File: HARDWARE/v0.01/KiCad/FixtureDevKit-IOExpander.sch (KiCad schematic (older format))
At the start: 58 parts, among them J57 IOExp_0, J58 IOExp_0, J59 Conn_01x24, J60 IOExp_1, J61 IOExp_1, J62 Conn_01x24, U5 TCA6426A, U6 TCA6426A

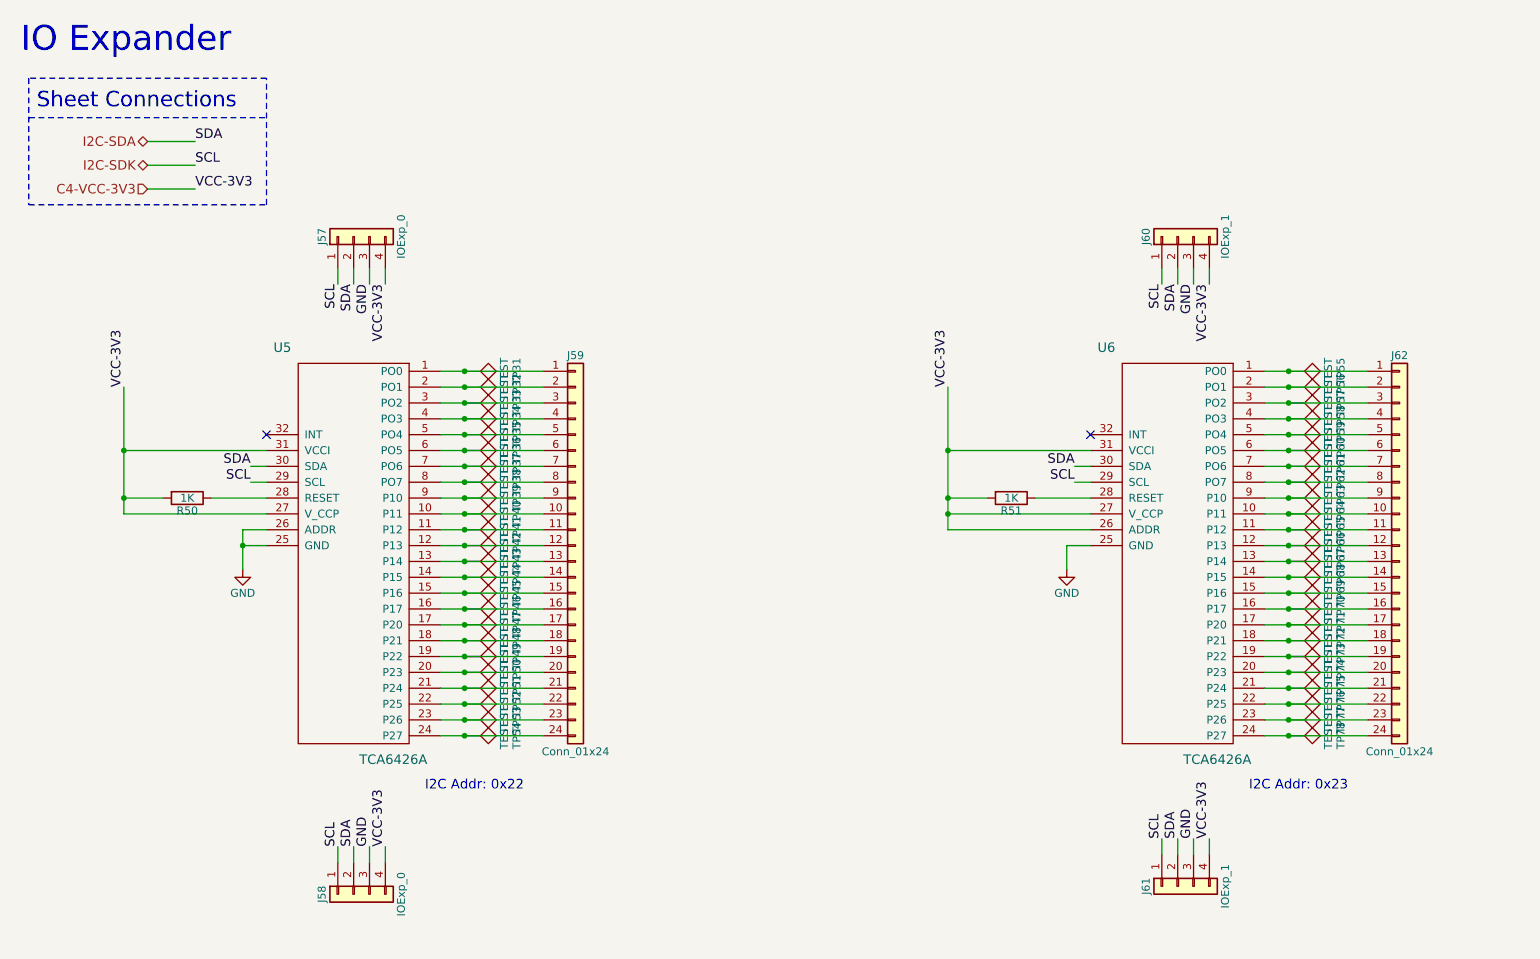
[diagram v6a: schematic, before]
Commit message: adding footprints, starting layout
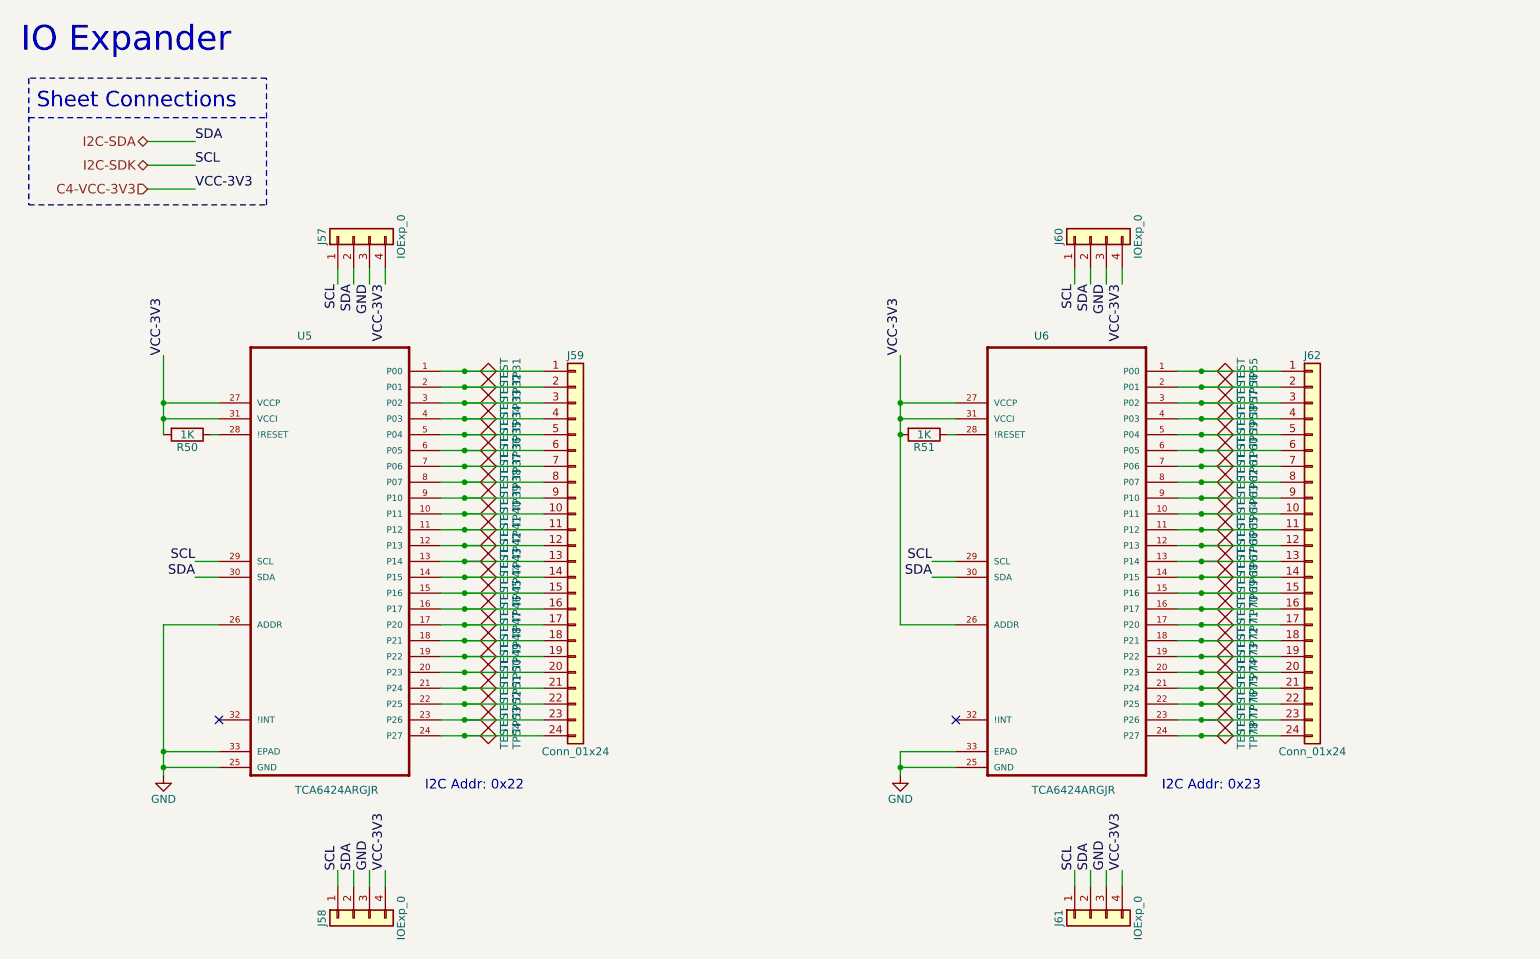
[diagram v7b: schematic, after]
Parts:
- removed U5, U6: TCA6426A, symbol TCA6426A
- added U5, U6: TCA6424ARGJR, TCA6424ARGJR:QFN50P500X500X60-33N, symbol TCA6424ARGJR
- J60, J61: value IOExp_1 -> IOExp_0
- TP31, TP32, TP33, TP34, TP35, TP36, TP37, TP38, TP39, TP40, TP41, TP42, TP43, TP44, TP45, TP46, TP47, TP48, TP49, TP50, TP51, TP52, TP53, TP54, TP55, TP56, TP57, TP58, TP59, TP60, TP61, TP62, TP63, TP64, TP65, TP66, TP67, TP68, TP69, TP70, TP71, TP72, TP73, TP74, TP75, TP76, TP77, TP78: footprint (none) -> TestPoint:TestPoint
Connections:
- net C4-VCC-3V3: now also U5.27 (VCCP), U5.31 (VCCI), U6.26 (ADDR), U6.27 (VCCP), U6.31 (VCCI)
- net GND: now also U5.25 (GND), U5.26 (ADDR), U5.33 (EPAD), U6.25 (GND), U6.33 (EPAD)
- net I2C-SDA: now also U5.30 (SDA), U6.30 (SDA)
- net I2C-SDK: now also U5.29 (SCL), U6.29 (SCL)
- net at J59.1 (Pin_1), TP31.1: now also U5.1 (P00)
- net at J59.10 (Pin_10), TP40.1: now also U5.10 (P11)
- net at J59.11 (Pin_11), TP41.1: now also U5.11 (P12)
- net at J59.12 (Pin_12), TP42.1: now also U5.12 (P13)
- net at J59.13 (Pin_13), TP43.1: now also U5.13 (P14)
- net at J59.14 (Pin_14), TP44.1: now also U5.14 (P15)
- net at J59.15 (Pin_15), TP45.1: now also U5.15 (P16)
- net at J59.16 (Pin_16), TP46.1: now also U5.16 (P17)
- net at J59.17 (Pin_17), TP47.1: now also U5.17 (P20)
- net at J59.18 (Pin_18), TP48.1: now also U5.18 (P21)
- net at J59.19 (Pin_19), TP49.1: now also U5.19 (P22)
- net at J59.2 (Pin_2), TP32.1: now also U5.2 (P01)
- net at J59.20 (Pin_20), TP50.1: now also U5.20 (P23)
- net at J59.21 (Pin_21), TP51.1: now also U5.21 (P24)
- net at J59.22 (Pin_22), TP52.1: now also U5.22 (P25)
- net at J59.23 (Pin_23), TP53.1: now also U5.23 (P26)
- net at J59.24 (Pin_24), TP54.1: now also U5.24 (P27)
- net at R50.1: now also U5.28 (!RESET)
- net at J59.3 (Pin_3), TP33.1: now also U5.3 (P02)
- net at J59.4 (Pin_4), TP34.1: now also U5.4 (P03)
- net at J59.5 (Pin_5), TP35.1: now also U5.5 (P04)
- net at J59.6 (Pin_6), TP36.1: now also U5.6 (P05)
- net at J59.7 (Pin_7), TP37.1: now also U5.7 (P06)
- net at J59.8 (Pin_8), TP38.1: now also U5.8 (P07)
- net at J59.9 (Pin_9), TP39.1: now also U5.9 (P10)
- net at J62.1 (Pin_1), TP55.1: now also U6.1 (P00)
- net at J62.10 (Pin_10), TP64.1: now also U6.10 (P11)
- net at J62.11 (Pin_11), TP65.1: now also U6.11 (P12)
- net at J62.12 (Pin_12), TP66.1: now also U6.12 (P13)
- net at J62.13 (Pin_13), TP67.1: now also U6.13 (P14)
- net at J62.14 (Pin_14), TP68.1: now also U6.14 (P15)
- net at J62.15 (Pin_15), TP69.1: now also U6.15 (P16)
- net at J62.16 (Pin_16), TP70.1: now also U6.16 (P17)
- net at J62.17 (Pin_17), TP71.1: now also U6.17 (P20)
- net at J62.18 (Pin_18), TP72.1: now also U6.18 (P21)
- net at J62.19 (Pin_19), TP73.1: now also U6.19 (P22)
- net at J62.2 (Pin_2), TP56.1: now also U6.2 (P01)
- net at J62.20 (Pin_20), TP74.1: now also U6.20 (P23)
- net at J62.21 (Pin_21), TP75.1: now also U6.21 (P24)
- net at J62.22 (Pin_22), TP76.1: now also U6.22 (P25)
- net at J62.23 (Pin_23), TP77.1: now also U6.23 (P26)
- net at J62.24 (Pin_24), TP78.1: now also U6.24 (P27)
- net at R51.1: now also U6.28 (!RESET)
- net at J62.3 (Pin_3), TP57.1: now also U6.3 (P02)
- net at J62.4 (Pin_4), TP58.1: now also U6.4 (P03)
- net at J62.5 (Pin_5), TP59.1: now also U6.5 (P04)
- net at J62.6 (Pin_6), TP60.1: now also U6.6 (P05)
- net at J62.7 (Pin_7), TP61.1: now also U6.7 (P06)
- net at J62.8 (Pin_8), TP62.1: now also U6.8 (P07)
- net at J62.9 (Pin_9), TP63.1: now also U6.9 (P10)
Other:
- moved on the sheet: J58
